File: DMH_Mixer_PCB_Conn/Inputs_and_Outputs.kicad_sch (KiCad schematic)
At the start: 9 parts, among them J1 TS_Jack_6.35mm_Sw, J2 TS_Jack_6.35mm_Sw, J200 IDC_02x05, J3 TS_Jack_6.35mm_Sw, J4 TS_Jack_6.35mm_Sw, J5 TS_Jack_6.35mm_Sw, J50 Conn_01x08, J6 TS_Jack_6.35mm_Sw, J60 Conn_01x08

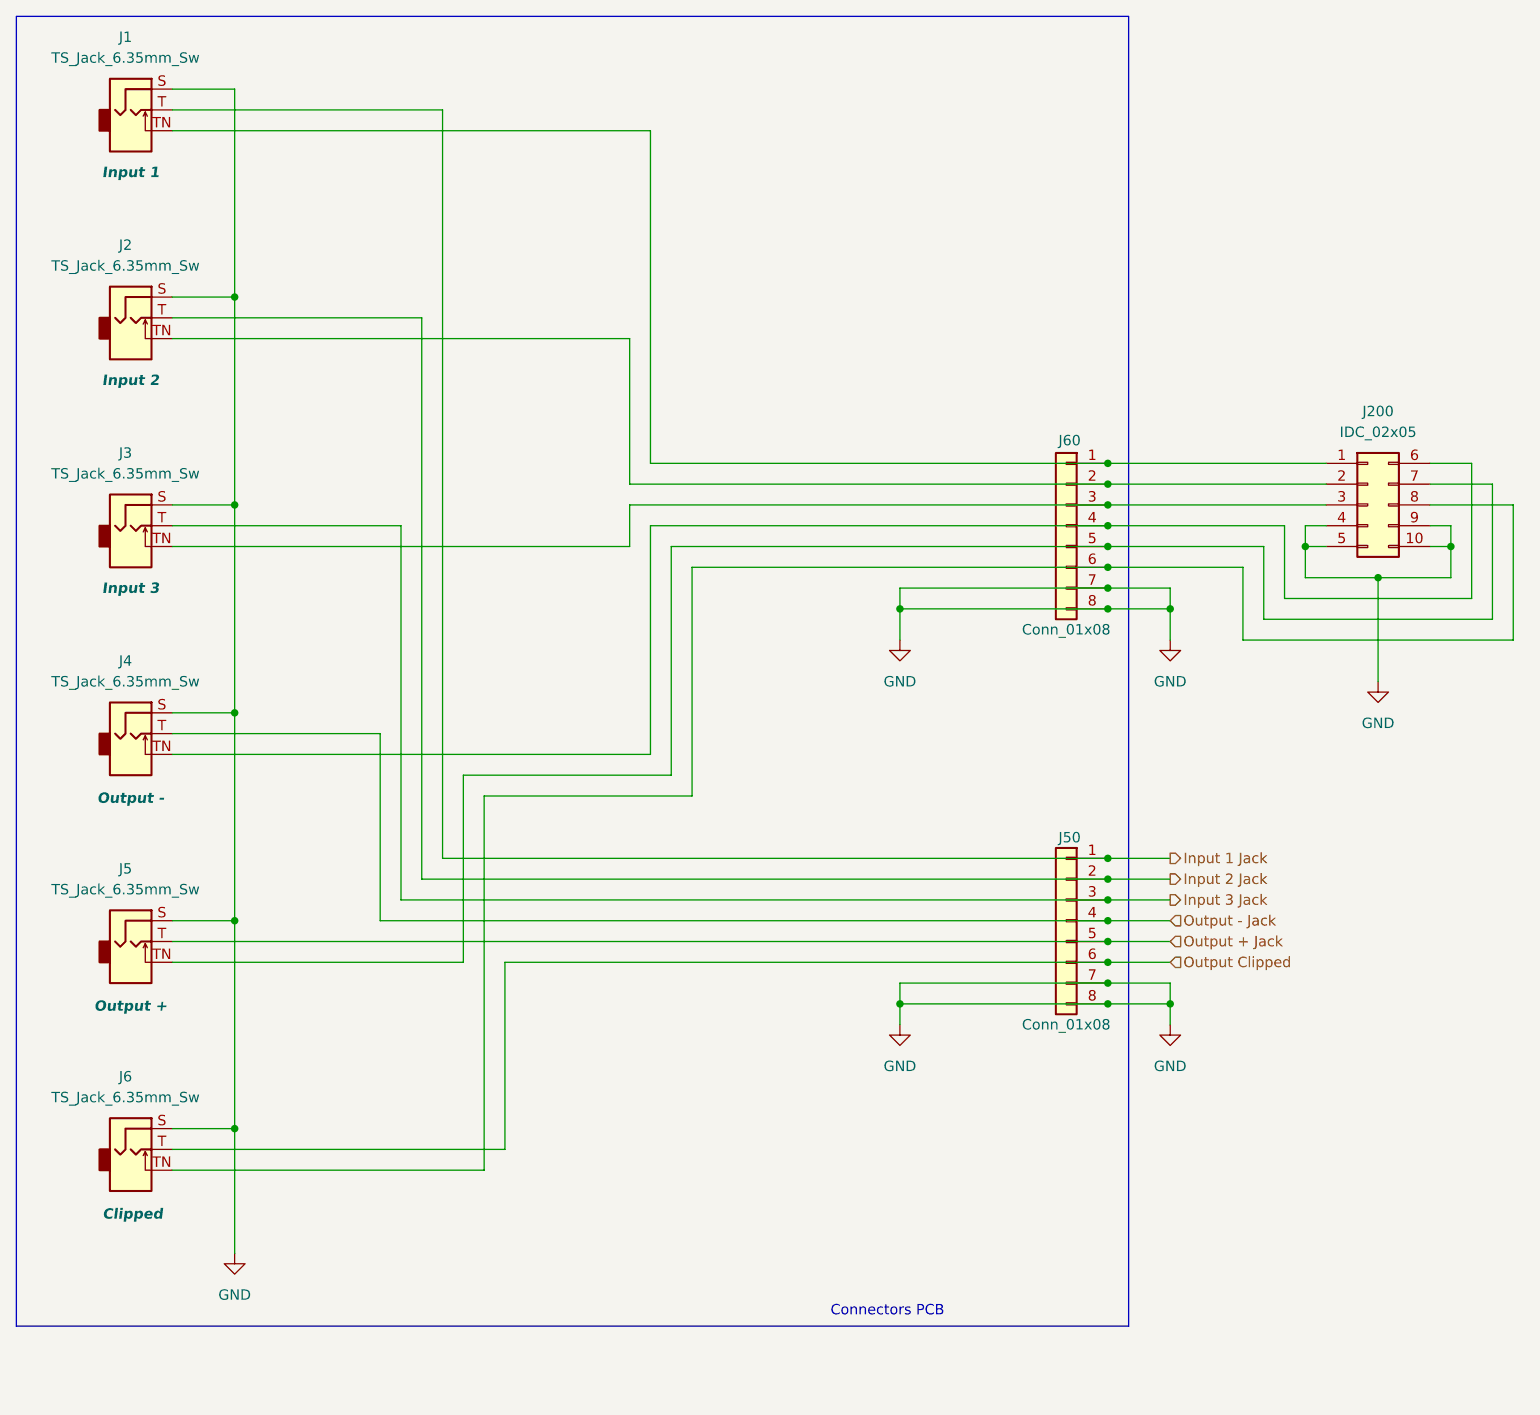
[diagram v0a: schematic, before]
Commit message: Adapted connectors PCB to 4 channel
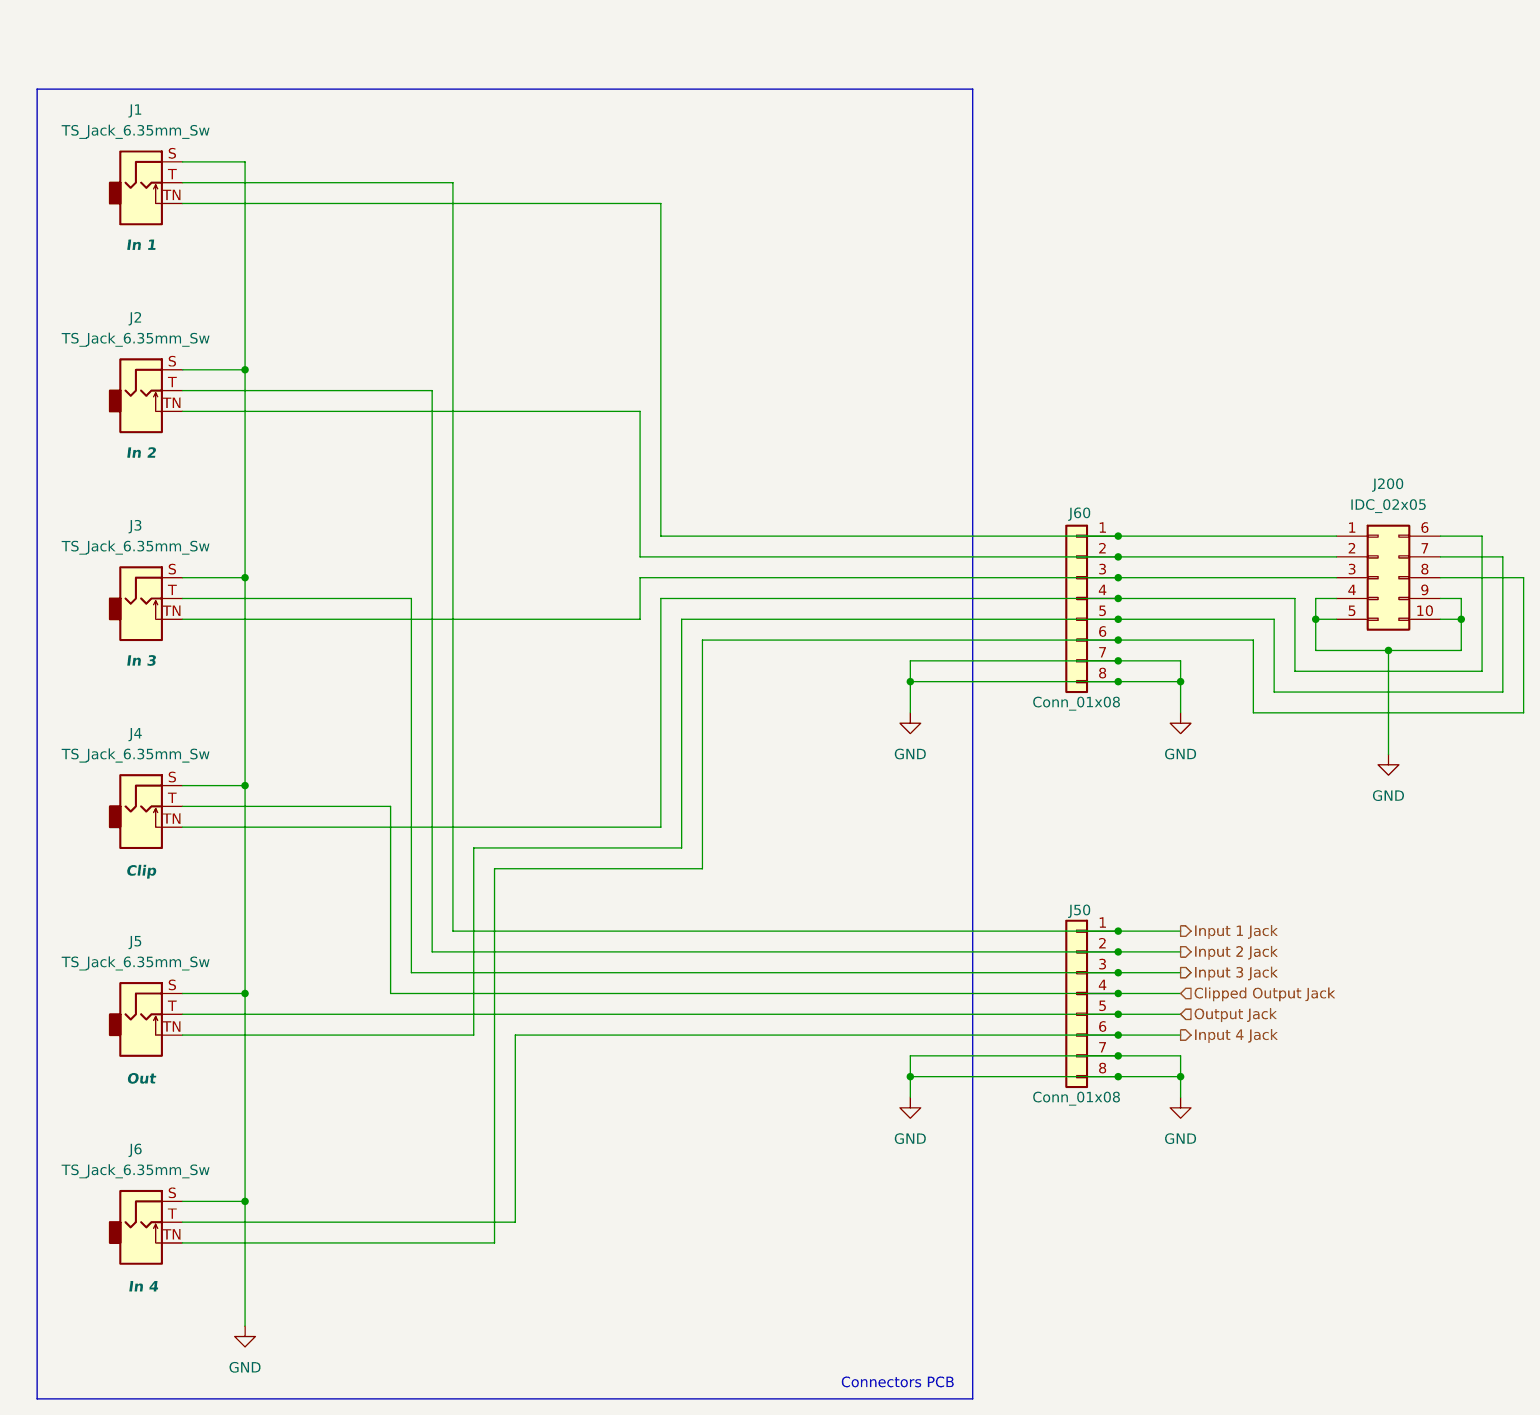
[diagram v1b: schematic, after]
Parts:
- J1: Function Input 1 -> In 1
- J2: Function Input 2 -> In 2
- J3: Function Input 3 -> In 3
- J4: Function Output - -> Clip
- J5: Function Output + -> Out
- J6: Function Clipped -> In 4
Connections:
- net Output + Jack renamed Output Jack
- net Output - Jack renamed Clipped Output Jack
- net Output Clipped renamed Input 4 Jack

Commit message: Moved output jacks to bottom right
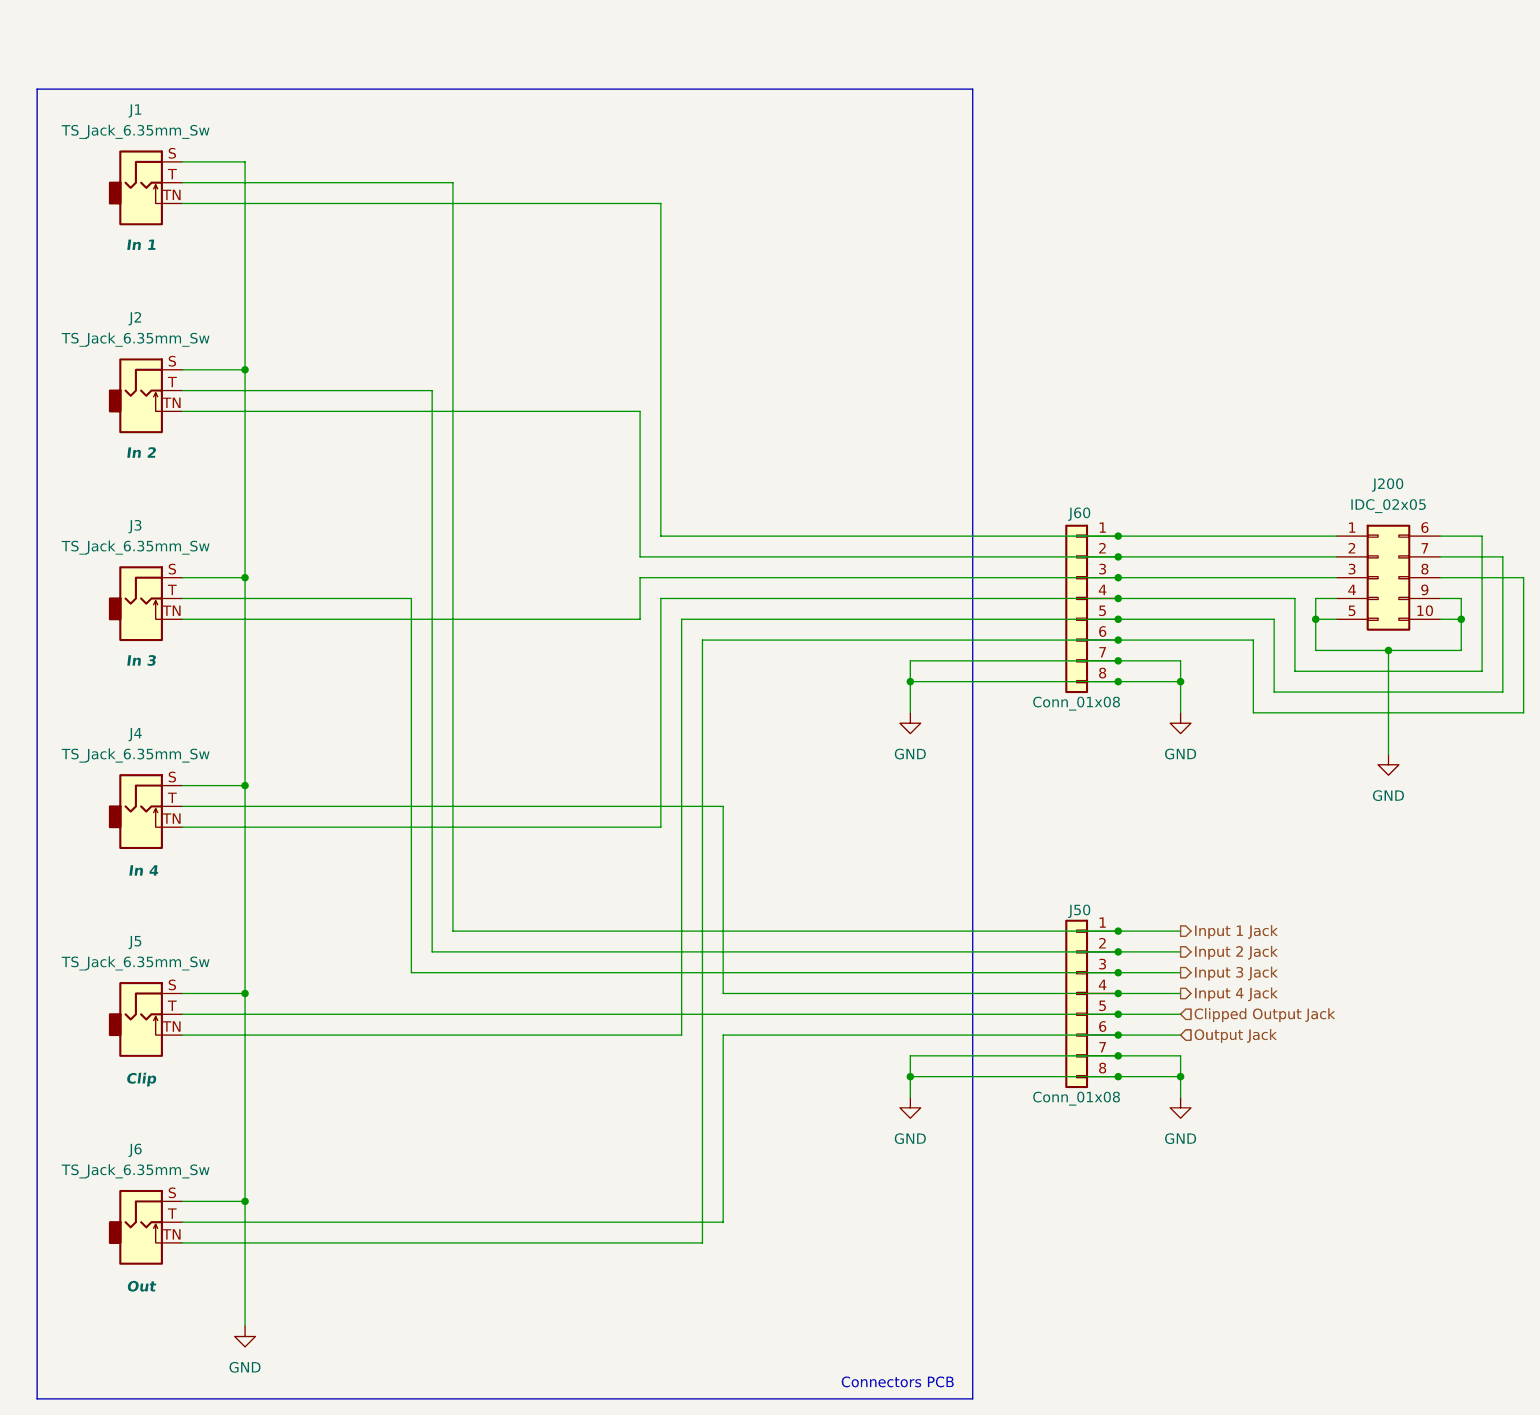
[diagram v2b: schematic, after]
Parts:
- renumbered J6 to J4, J4 to J5, J5 to J6
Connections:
- net Clipped Output Jack: now also J50.5 (Pin_5); no longer J50.4 (Pin_4)
- net Input 4 Jack: now also J50.4 (Pin_4); no longer J50.6 (Pin_6)
- net Output Jack: now also J50.6 (Pin_6); no longer J50.5 (Pin_5)
- net at J200.7 (Pin_7), J60.5 (Pin_5): now also J5.TN; no longer J6.TN
- net at J200.6 (Pin_6), J60.4 (Pin_4): now also J4.TN; no longer J5.TN
- net at J200.8 (Pin_8), J60.6 (Pin_6): now also J6.TN; no longer J4.TN
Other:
- moved on the sheet: J4, J5, J6
